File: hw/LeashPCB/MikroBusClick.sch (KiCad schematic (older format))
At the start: 2 parts, among them J701 mikroBUS, J702 mikroBUS

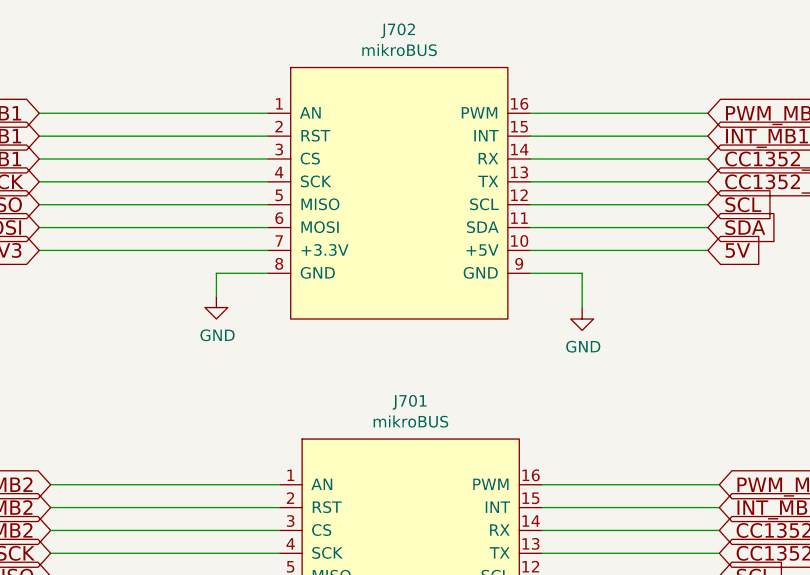
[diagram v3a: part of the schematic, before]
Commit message: Removed two extra pullup resistors
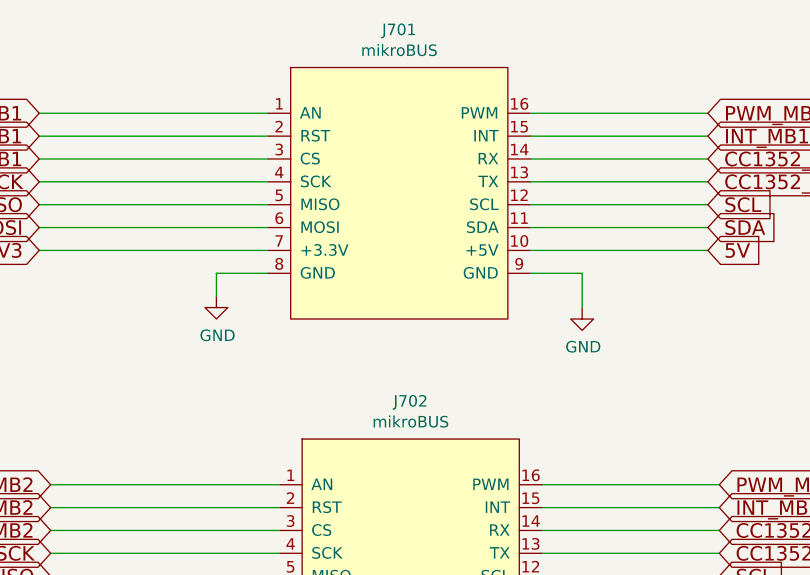
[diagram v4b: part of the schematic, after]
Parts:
- renumbered J702 to J701, J701 to J702
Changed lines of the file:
@@
 P 8675 4025
 AR Path="/5D092D9C" Ref="J?"  Part="1"
-AR Path="/5D066680/5D092D9C" Ref="J702"  Part="1"
-F 0 "J702" H 8700 4740 50  0000 C CNN
+AR Path="/5D066680/5D092D9C" Ref="J701"  Part="1"
+F 0 "J701" H 8700 4740 50  0000 C CNN
 F 1 "mikroBUS" H 8700 4649 50  0000 C CNN
 F 2 "leash:MikroBus-SMD" H 8475 4225 50  0001 C CNN
@@
 	7900 4375 7900 4475
 $Comp
-L power:GND #PWR0104
+L power:GND #PWR0701
 U 1 1 5D1F9F78
 P 7900 4475
-F 0 "#PWR0104" H 7900 4225 50  0001 C CNN
+F 0 "#PWR0701" H 7900 4225 50  0001 C CNN
 F 1 "GND" H 7905 4302 50  0000 C CNN
 F 2 "" H 7900 4475 50  0001 C CNN
@@
 	9275 4275 10050 4275
 $Comp
-L power:GND #PWR0105
+L power:GND #PWR0703
 U 1 1 5D200D92
 P 9500 4525
-F 0 "#PWR0105" H 9500 4275 50  0001 C CNN
+F 0 "#PWR0703" H 9500 4275 50  0001 C CNN
 F 1 "GND" H 9505 4352 50  0000 C CNN
 F 2 "" H 9500 4525 50  0001 C CNN
@@
 P 8725 5650
 AR Path="/5E8910E4" Ref="J?"  Part="1"
-AR Path="/5D066680/5E8910E4" Ref="J701"  Part="1"
-F 0 "J701" H 8750 6365 50  0000 C CNN
+AR Path="/5D066680/5E8910E4" Ref="J702"  Part="1"
+F 0 "J702" H 8750 6365 50  0000 C CNN
 F 1 "mikroBUS" H 8750 6274 50  0000 C CNN
 F 2 "leash:MikroBus-SMD" H 8525 5850 50  0001 C CNN
@@
 	7950 6000 7950 6100
 $Comp
-L power:GND #PWR0103
+L power:GND #PWR0702
 U 1 1 5E8910FE
 P 7950 6100
-F 0 "#PWR0103" H 7950 5850 50  0001 C CNN
+F 0 "#PWR0702" H 7950 5850 50  0001 C CNN
 F 1 "GND" H 7955 5927 50  0000 C CNN
 F 2 "" H 7950 6100 50  0001 C CNN
@@
 $EndComp
 $Comp
-L power:GND #PWR0120
+L power:GND #PWR0704
 U 1 1 5E89110F
 P 9550 6150
-F 0 "#PWR0120" H 9550 5900 50  0001 C CNN
+F 0 "#PWR0704" H 9550 5900 50  0001 C CNN
 F 1 "GND" H 9555 5977 50  0000 C CNN
 F 2 "" H 9550 6150 50  0001 C CNN

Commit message: Updated BOM for ordering parts
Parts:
- J701: Description N/A -> Order 2 of these connectors! Right tight top; Link1 https://www.digikey.com/product-detail/en/sullins-connector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 -> https://SZconnect.com; Link2 (none) -> https://www.digikey.com/product-detail/en/sullins-connector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; MPN1 NPTC081KFXC-RC -> ST-FH-254-0144-B; MPN2 (none) -> NPPC081KFXC-RC; Standard Price 0 -> 0.10; Value modifier (none) -> Need to buy in pairs!; Vendor1 Sullins -> Sinotop Electronics Ltd; Vendor2 (none) -> Sullins Connector Solutions
- J702: Link1 https://www.digikey.com/product-detail/en/sullins-connector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 -> https://SZconnect.com; Link2 (none) -> https://www.digikey.com/product-detail/en/sullins-connector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; MPN1 NPTC081KFXC-RC -> ST-FH-254-0144-B; MPN2 (none) -> NPPC081KFXC-RC; Standard Price 0 -> 0.10; Value modifier (none) -> Need to buy in pairs!; Vendor1 Sullins -> Sinotop Electronics Ltd; Vendor2 (none) -> Sullins Connector Solutions
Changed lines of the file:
@@
 Comment4 ""
 $EndDescr
-$Comp
-L LeashPCB:mikroBUS J?
-U 1 1 5D092D9C
-P 8675 4025
-AR Path="/5D092D9C" Ref="J?"  Part="1"
-AR Path="/5D066680/5D092D9C" Ref="J701"  Part="1"
-F 0 "J701" H 8700 4740 50  0000 C CNN
-F 1 "mikroBUS" H 8700 4649 50  0000 C CNN
-F 2 "leash:MikroBus-SMD" H 8475 4225 50  0001 C CNN
-F 3 "" H 8475 4225 50  0001 C CNN
-F 4 "0" H 8675 4025 50  0001 C CNN "Standard Price"
-F 5 "N/A" H 8675 4025 50  0001 C CNN "Description"
-F 6 "https://www.digikey.com/product-detail/en/sullins-connector-solutions/NPTC081KFXC-RC/S5600-ND/776058" H 8675 4025 50  0001 C CNN "Link1"
-F 7 "NPTC081KFXC-RC" H 8675 4025 50  0001 C CNN "MPN1"
-F 8 "Sullins" H 8675 4025 50  0001 C CNN "Vendor1"
-F 9 "CONN HDR 8POS 0.1 TIN SMD" H 8675 4025 50  0001 C CNN "Short Description"
-	1    8675 4025
-	1    0    0    -1
-$EndComp
 Wire Wire Line
 	8125 4375 7900 4375
@@
 F 2 "leash:MikroBus-SMD" H 8525 5850 50  0001 C CNN
 F 3 "" H 8525 5850 50  0001 C CNN
-F 4 "0" H 8725 5650 50  0001 C CNN "Standard Price"
+F 4 "0.10" H 8725 5650 50  0001 C CNN "Standard Price"
 F 5 "N/A" H 8725 5650 50  0001 C CNN "Description"
-F 6 "https://www.digikey.com/product-detail/en/sullins-connector-solutions/NPTC081KFXC-RC/S5600-ND/776058" H 8725 5650 50  0001 C CNN "Link1"
-F 7 "NPTC081KFXC-RC" H 8725 5650 50  0001 C CNN "MPN1"
-F 8 "Sullins" H 8725 5650 50  0001 C CNN "Vendor1"
+F 6 "https://SZconnect.com" H 8725 5650 50  0001 C CNN "Link1"
+F 7 "ST-FH-254-0144-B" H 8725 5650 50  0001 C CNN "MPN1"
+F 8 "Sinotop Electronics Ltd" H 8725 5650 50  0001 C CNN "Vendor1"
 F 9 "CONN HDR 8POS 0.1 TIN SMD" H 8725 5650 50  0001 C CNN "Short Description"
+F 10 "https://www.digikey.com/product-detail/en/sullins-connector-solutions/NPPC081KFXC-RC/S5639-ND/776098" H 8725 5650 50  0001 C CNN "Link2"
+F 11 "NPPC081KFXC-RC" H 8725 5650 50  0001 C CNN "MPN2"
+F 12 "Need to buy in pairs!" H 8725 5650 50  0001 C CNN "Value modifier"
+F 13 "Sullins Connector Solutions" H 8725 5650 50  0001 C CNN "Vendor2"
 	1    8725 5650
 	1    0    0    -1
@@
 Wire Wire Line
 	8175 5900 7175 5900
+$Comp
+L LeashPCB:mikroBUS J?
+U 1 1 5D092D9C
+P 8675 4025
+AR Path="/5D092D9C" Ref="J?"  Part="1"
+AR Path="/5D066680/5D092D9C" Ref="J701"  Part="1"
+F 0 "J701" H 8700 4740 50  0000 C CNN
+F 1 "mikroBUS" H 8700 4649 50  0000 C CNN
+F 2 "leash:MikroBus-SMD" H 8475 4225 50  0001 C CNN
+F 3 "" H 8475 4225 50  0001 C CNN
+F 4 "0.10" H 8675 4025 50  0001 C CNN "Standard Price"
+F 5 "Order 2 of these connectors! Right tight top" H 8675 4025 50  0001 C CNN "Description"
+F 6 "https://SZconnect.com" H 8675 4025 50  0001 C CNN "Link1"
+F 7 "ST-FH-254-0144-B" H 8675 4025 50  0001 C CNN "MPN1"
+F 8 "Sinotop Electronics Ltd" H 8675 4025 50  0001 C CNN "Vendor1"
+F 9 "CONN HDR 8POS 0.1 TIN SMD" H 8675 4025 50  0001 C CNN "Short Description"
+F 10 "https://www.digikey.com/product-detail/en/sullins-connector-solutions/NPPC081KFXC-RC/S5639-ND/776098" H 8675 4025 50  0001 C CNN "Link2"
+F 11 "NPPC081KFXC-RC" H 8675 4025 50  0001 C CNN "MPN2"
+F 12 "Need to buy in pairs!" H 8675 4025 50  0001 C CNN "Value modifier"
+F 13 "Sullins Connector Solutions" H 8675 4025 50  0001 C CNN "Vendor2"
+	1    8675 4025
+	1    0    0    -1
+$EndComp
 $EndSCHEMATC
